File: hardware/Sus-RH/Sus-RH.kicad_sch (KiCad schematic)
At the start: 29 parts, among them J1 Conn_01x06, J2 Conn_01x04, J3 Conn_01x04, J4 Conn_01x04, J5 Conn_01x06, J6 Conn_01x03, J7 53307-2471

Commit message: finished layout + silkscreen, ready to review.
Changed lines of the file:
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@@
-		)
-	)
-	(text_box "MX150 Connector\n"
-		(exclude_from_sim no)
-		(at 283.21 241.3 0)
-		(size 105.41 78.74)
-		(margins 0.9525 0.9525 0.9525 0.9525)
-		(stroke
-			(width 0)
-			(type solid)
-		)
-		(fill
-			(type none)
-		)
-		(effects
-			(font
-				(size 1.27 1.27)
-			)
-			(justify left top)
 		)
 	)

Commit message: made changes from review council
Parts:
- removed J2: Conn_01x04, Connector_Molex:Molex_Nano-Fit_105314-xx04_2x02_P2.50mm_Horizontal, symbol Connector_Generic:Conn_01x04
- removed J3, J4: Conn_01x04, Connector_Molex:Molex_Nano-Fit_105313-xx04_1x04_P2.50mm_Horizontal, symbol Connector_Generic:Conn_01x04
- added J2, J3, J4: Conn_01x05, Connector_Molex:Molex_Nano-Fit_105313-xx05_1x05_P2.50mm_Horizontal, symbol Connector_Generic:Conn_01x05
- added R15, R16, R17: 0, Resistor_SMD:R_0603_1608Metric_Pad0.98x0.95mm_HandSolder, symbol Device:R
- GND1: footprint TestPoint:TestPoint_Pad_1.0x1.0mm -> TestPoint:TestPoint_THTPad_2.5x2.5mm_Drill1.2mm
- GNDA1: footprint TestPoint:TestPoint_Pad_1.0x1.0mm -> TestPoint:TestPoint_THTPad_1.5x1.5mm_Drill0.7mm
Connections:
- net +24V: now also J2.1 (Pin_1), J3.1 (Pin_1), J4.1 (Pin_1)
- net CAN_+: now also J2.2 (Pin_2), J3.2 (Pin_2), J4.2 (Pin_2)
- net CAN_-: now also J2.3 (Pin_3), J3.3 (Pin_3), J4.3 (Pin_3)
- net GND: now also J2.4 (Pin_4), J3.4 (Pin_4), J4.4 (Pin_4), R15.1, R16.1, R17.1
- new net: J3.5 (Pin_5), R15.2
- new net: J2.5 (Pin_5), R17.2
- new net: J4.5 (Pin_5), R16.2
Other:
- moved on the sheet: F1, F2, J5, J6

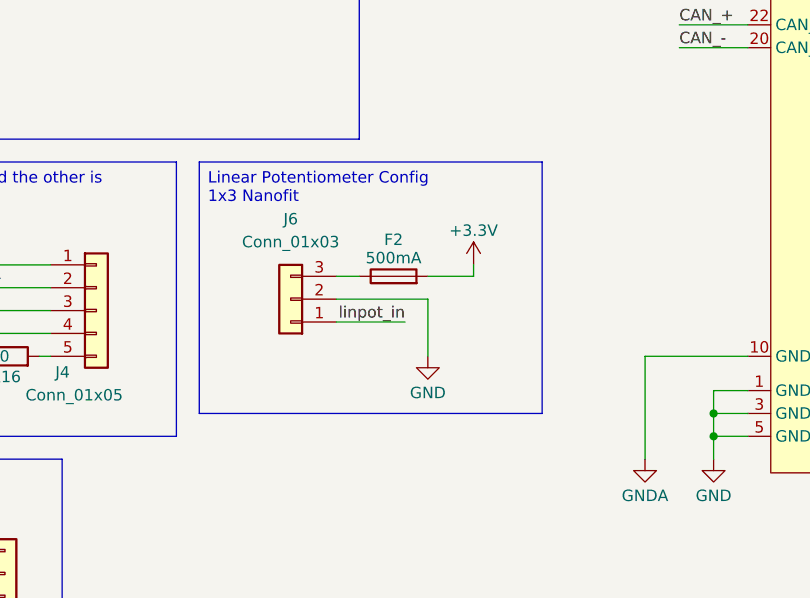
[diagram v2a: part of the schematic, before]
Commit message: fixed nanofit for linpot
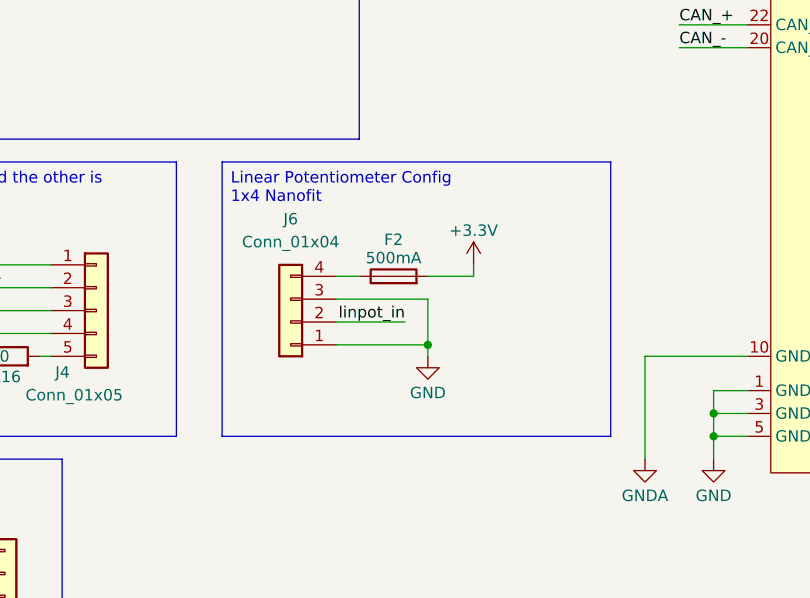
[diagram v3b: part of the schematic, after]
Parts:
- removed J6: Conn_01x03, Connector_Molex:Molex_Nano-Fit_105313-xx03_1x03_P2.50mm_Horizontal, symbol Connector_Generic:Conn_01x03
- added J6: Conn_01x04, Connector_Molex:Molex_Nano-Fit_105313-xx04_1x04_P2.50mm_Horizontal, symbol Connector_Generic:Conn_01x04
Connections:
- net GND: now also J6.1 (Pin_1), J6.3 (Pin_3)
- net linpot_in: now also J6.2 (Pin_2)
- net at F2.1: now also J6.4 (Pin_4)
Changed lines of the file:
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@@
 		)
 	)
-	(text_box "Linear Potentiometer Config\n1x3 Nanofit\n"
+	(text_box "Linear Potentiometer Config\n1x4 Nanofit\n"
 		(exclude_from_sim no)
-		(at 149.86 50.8 0)
-		(size 38.1 27.94)
+		(at 152.4 50.8 0)
+		(size 43.18 30.48)
 		(margins 0.9525 0.9525 0.9525 0.9525)
 		(stroke
@@
 	)
 	(junction
+		(at 175.26 71.12)
+		(diameter 0)
+		(color 0 0 0 0)
+	)
+	(junction
 		(at 275.59 40.64)
 		(diameter 0)
@@
 	(wire
 		(pts
+			(xy 165.1 71.12) (xy 175.26 71.12)
+		)
+		(stroke
+			(width 0)
+			(type default)
+		)
+	)
+	(wire
+		(pts
 			(xy 265.43 27.94) (xy 265.43 29.21)
 		)
@@
 	(wire
 		(pts
+			(xy 175.26 71.12) (xy 175.26 72.39)
+		)
+		(stroke
+			(width 0)
+			(type default)
+		)
+	)
+	(wire
+		(pts
 			(xy 74.93 140.97) (xy 74.93 143.51)
 		)
@@
 	(wire
 		(pts
-			(xy 175.26 66.04) (xy 175.26 72.39)
+			(xy 175.26 66.04) (xy 175.26 71.12)
 		)
 		(stroke
@@
 	)
 	(symbol
-		(lib_id "Connector_Generic:Conn_01x03")
-		(at 160.02 66.04 180)
-		(unit 1)
-		(exclude_from_sim no)
-		(in_bom yes)
-		(on_board yes)
-		(dnp no)
-		(fields_autoplaced yes)
-		(property "Reference" "J6"
-			(at 160.02 57.15 0)
-			(effects
-				(font
-					(size 1.27 1.27)
-				)
-			)
-		)
-		(property "Value" "Conn_01x03"
-			(at 160.02 59.69 0)
-			(effects
-				(font
-					(size 1.27 1.27)
-				)
-			)
-		)
-		(property "Footprint" "Connector_Molex:Molex_Nano-Fit_105313-xx03_1x03_P2.50mm_Horizontal"
-			(at 160.02 66.04 0)
-			(effects
-				(font
-					(size 1.27 1.27)
-				)
-				(hide yes)
-			)
-		)
-		(property "Datasheet" "~"
-			(at 160.02 66.04 0)
-			(effects
-				(font
-					(size 1.27 1.27)
-				)
-				(hide yes)
-			)
-		)
-		(property "Description" "Generic connector, single row, 01x03, script generated (kicad-library-utils/schlib/autogen/connector/)"
-			(at 160.02 66.04 0)
-			(effects
-				(font
-					(size 1.27 1.27)
-				)
-				(hide yes)
-			)
-		)
-		(pin "1"
-		)
-		(pin "2"
-		)
-		(pin "3"
-		)
-		(instances
-			(project ""
-				(path "/5f8d513b-42c2-4d15-b515-d2d66a528ded"
-					(reference "J6")
-					(unit 1)
-				)
-			)
-		)
-	)
-	(symbol
 		(lib_id "Connector:TestPoint")
 		(at 34.29 91.44 270)
@@
 					(unit 1)
 				)
+			)
+		)
+	)
+	(symbol
+		(lib_id "Connector_Generic:Conn_01x04")
+		(at 160.02 68.58 180)
+		(unit 1)
+		(exclude_from_sim no)
+		(in_bom yes)
+		(on_board yes)
+		(dnp no)
+		(fields_autoplaced yes)
+		(property "Reference" "J6"
+			(at 160.02 57.15 0)
+			(effects
+				(font
+					(size 1.27 1.27)
+				)
+			)
+		)
+		(property "Value" "Conn_01x04"
+			(at 160.02 59.69 0)
+			(effects
+				(font
+					(size 1.27 1.27)
+				)
+			)
+		)
+		(property "Footprint" "Connector_Molex:Molex_Nano-Fit_105313-xx04_1x04_P2.50mm_Horizontal"
+			(at 160.02 68.58 0)
+			(effects
+				(font
+					(size 1.27 1.27)
+				)
+				(hide yes)
+			)
+		)
+		(property "Datasheet" "~"
+			(at 160.02 68.58 0)
+			(effects
+				(font
+					(size 1.27 1.27)
+				)
+				(hide yes)
+			)
+		)
+		(property "Description" "Generic connector, single row, 01x04, script generated (kicad-library-utils/schlib/autogen/connector/)"
+			(at 160.02 68.58 0)
+			(effects
+				(font
+					(size 1.27 1.27)
+				)
+				(hide yes)
+			)
+		)
+		(pin "1"
+		)
+		(pin "2"
+		)
+		(pin "3"
+		)
+		(pin "4"
+		)
+		(instances
+			(project ""
+				(path "/5f8d513b-42c2-4d15-b515-d2d66a528ded"
+					(reference "J6")
+					(unit 1)
+				)
